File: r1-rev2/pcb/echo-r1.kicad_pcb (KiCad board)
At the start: 6 copper layers, 52 x 94 mm, 22 parts, among them J2 TYPE-C-31-M-12, J4 HP_3.5mm, J5 LO_3.5mm, SW1 A, SW10 SELECT, SW11 VOL+, SW12 VOL-, SW13 POWER, SW14 HOLD, SW2 B, SW3 X, SW4 Y, SW5 DPAD↑, SW6 DPAD↓, SW7 DPAD←, SW8 DPAD→, SW9 START

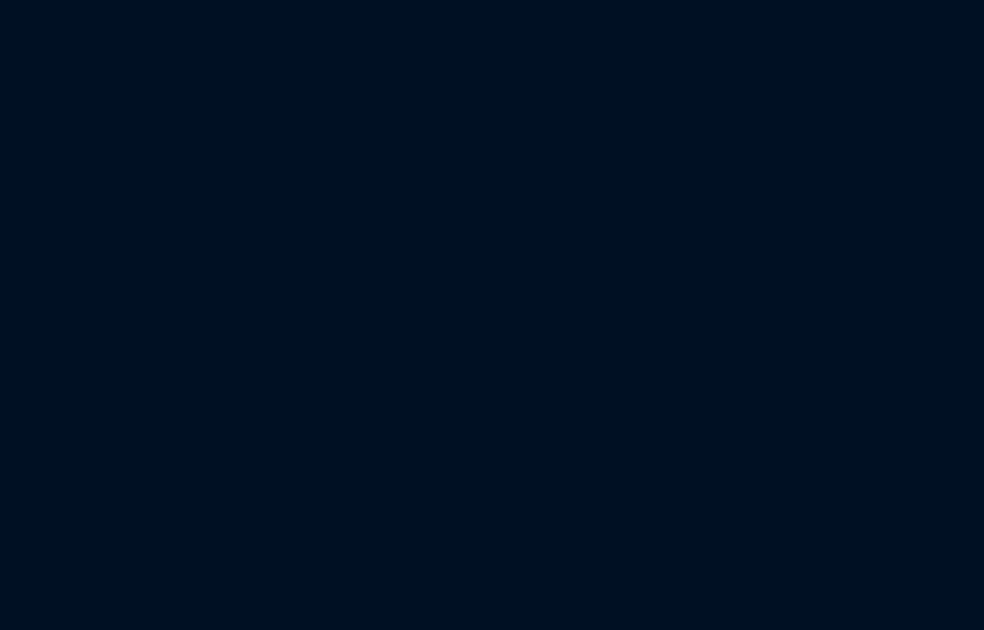
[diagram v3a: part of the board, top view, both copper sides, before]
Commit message: R1-Rev2: add LCD ribbon connector
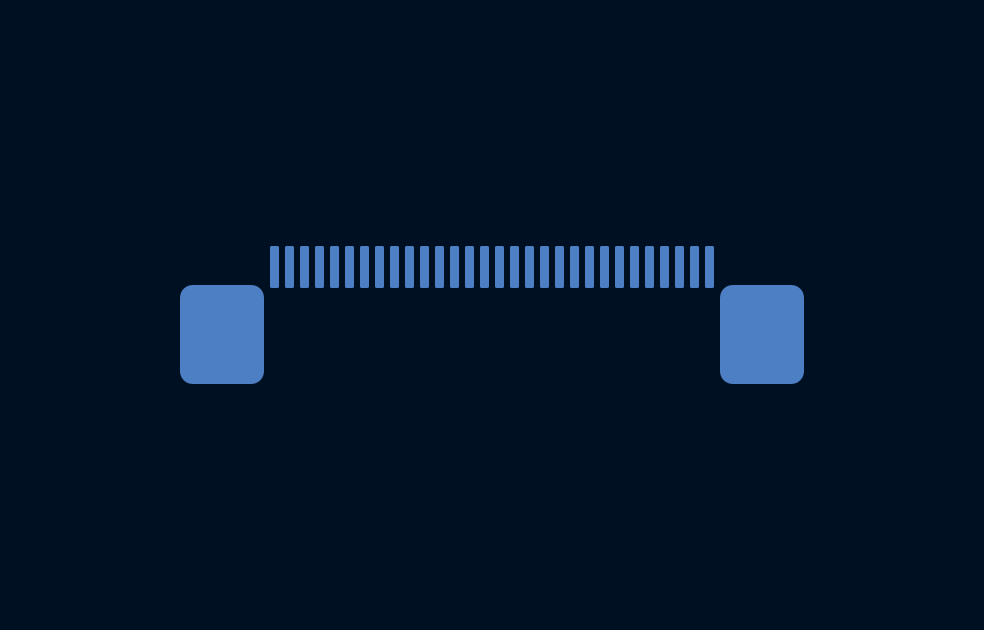
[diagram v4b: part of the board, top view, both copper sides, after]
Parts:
- added J7: AFC07-S30ECA-00, echoplayer:Conn_Jushuo_AFC07-S30ECA-00_RTL, B.Cu at (147.5, 74.3)

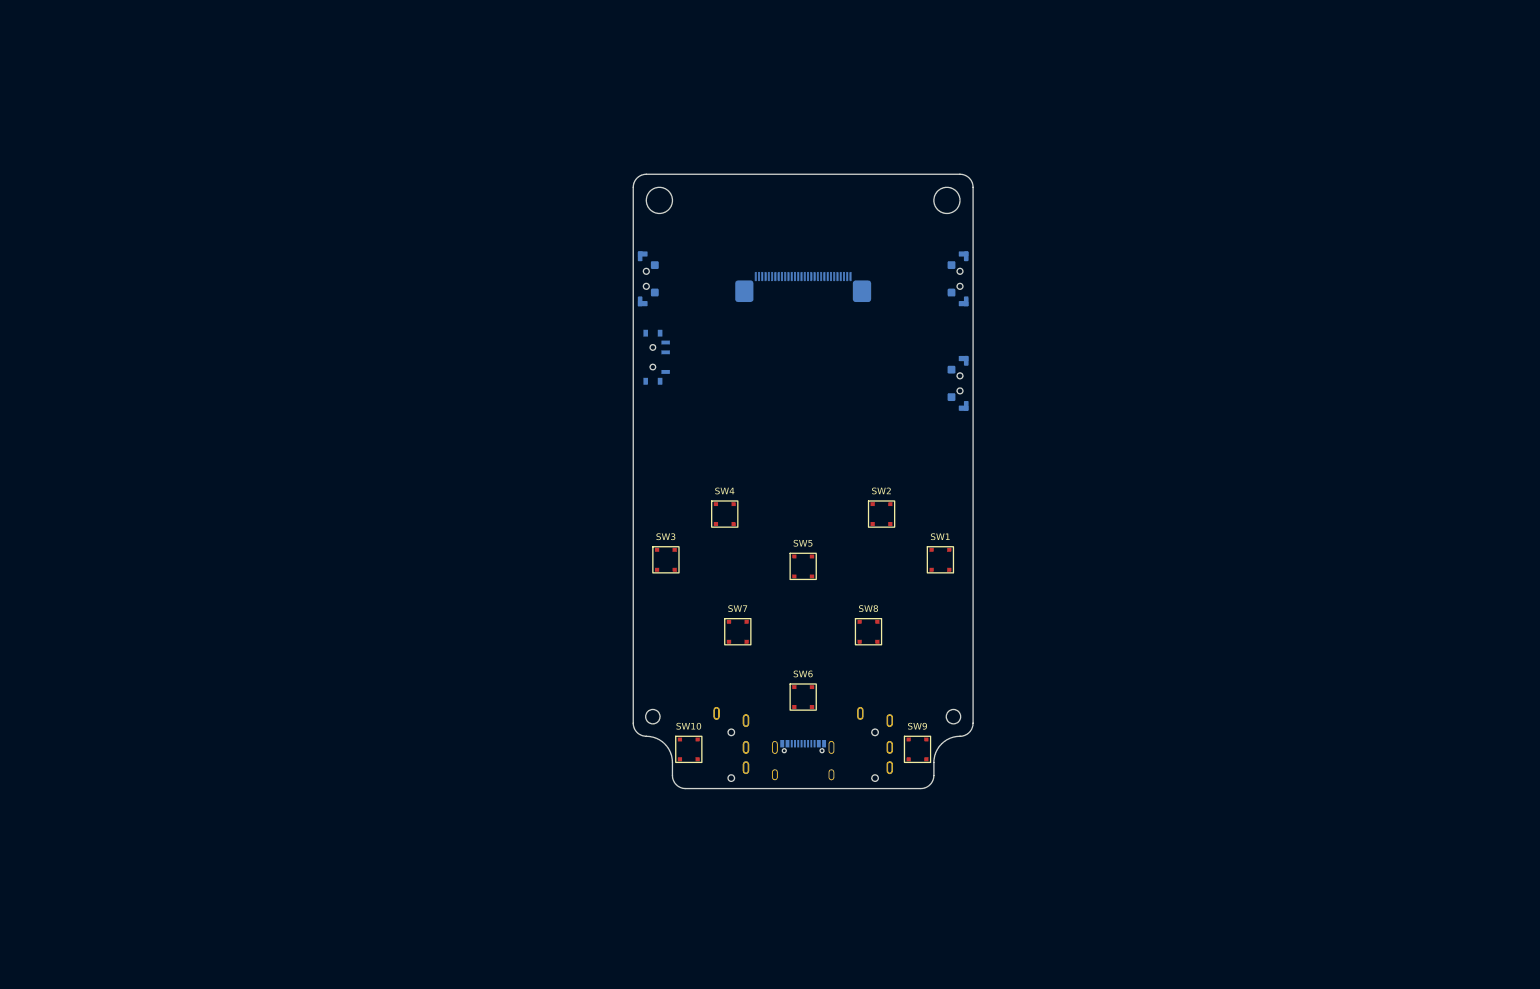
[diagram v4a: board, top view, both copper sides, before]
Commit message: R1-Rev2: updates to PCB layout, add HyperRAM routing
- Reannotate schematic and assign footprints for passives
- First try at HyperRAM routing
- Fixed incorrect W958D8NBYA5I pinout
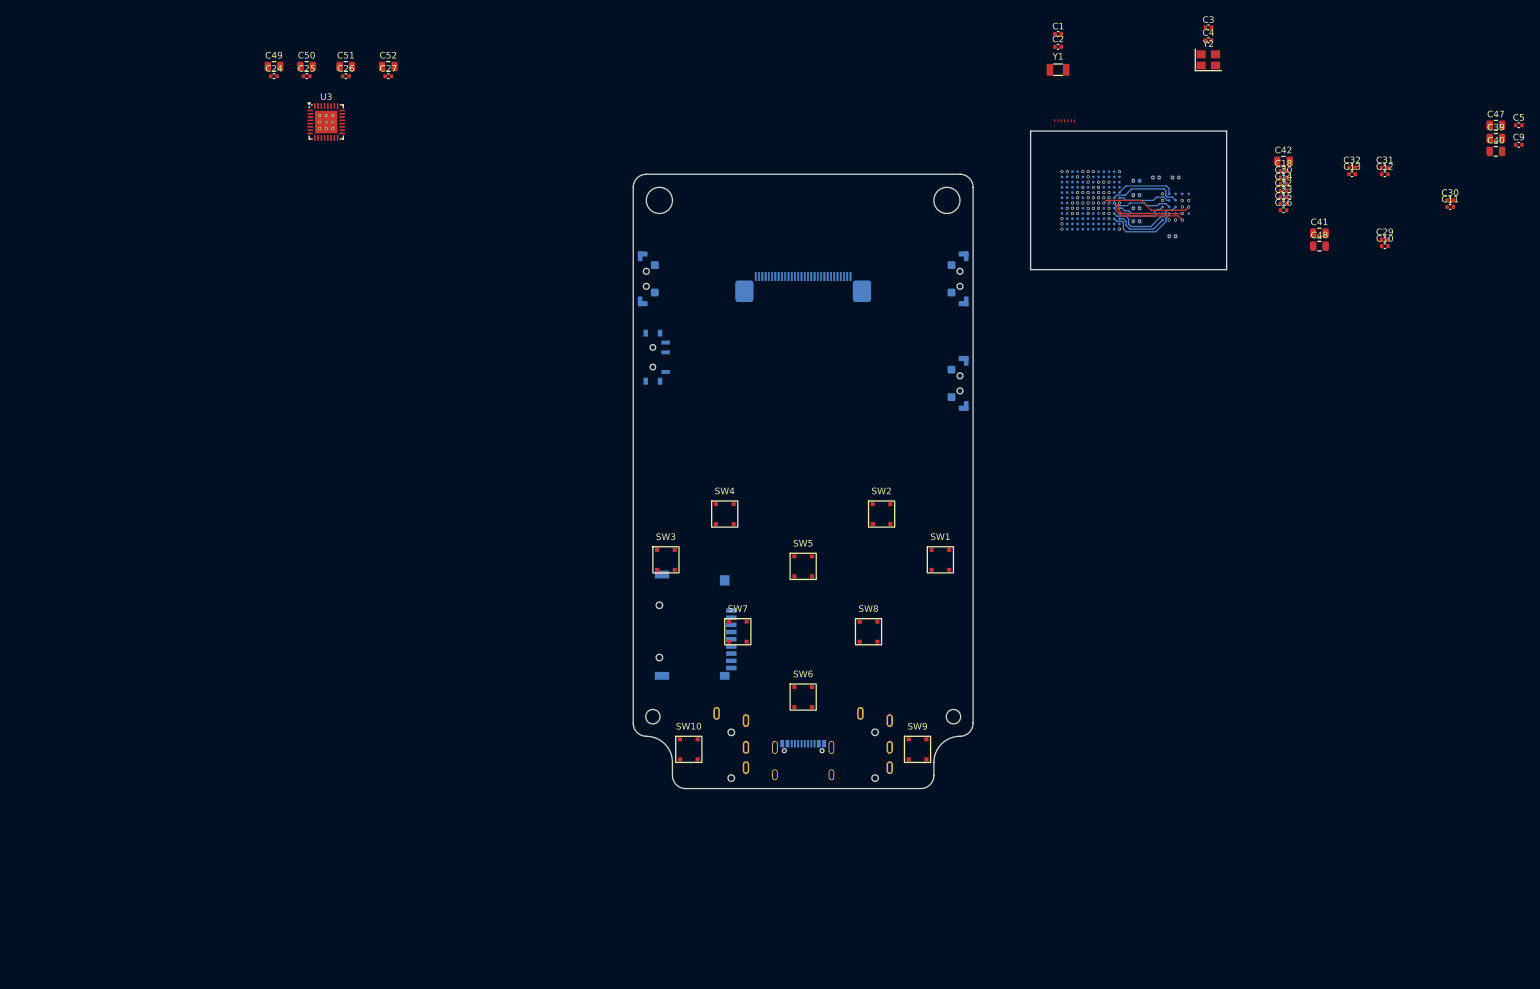
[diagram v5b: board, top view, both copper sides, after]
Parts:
- added C1: 10 pF, Capacitor_SMD:C_0402_1005Metric, F.Cu at (186.5, 36.5)
- added C10: 100 nF, Capacitor_SMD:C_0402_1005Metric, F.Cu at (236.5, 69.0)
- added C11: 100 nF, Capacitor_SMD:C_0402_1005Metric, F.Cu at (246.5, 63.0)
- added C12: 100 nF, Capacitor_SMD:C_0402_1005Metric, F.Cu at (236.5, 58.0)
- added C13: 100 nF, Capacitor_SMD:C_0402_1005Metric, F.Cu at (231.5, 58.0)
- added C14: 100 nF, Capacitor_SMD:C_0402_1005Metric, F.Cu at (221.0, 59.5)
- added C15: 100 nF, Capacitor_SMD:C_0402_1005Metric, F.Cu at (221.0, 62.5)
- added C16: 100 nF, Capacitor_SMD:C_0402_1005Metric, F.Cu at (221.0, 63.5)
- added C17: 100 nF, Capacitor_SMD:C_0402_1005Metric, B.Cu at (198.5, 65.2)
- added C18: 100 nF, Capacitor_SMD:C_0402_1005Metric, F.Cu at (221.0, 57.5)
- added C19: 100 nF, Capacitor_SMD:C_0402_1005Metric, B.Cu at (198.5, 63.2)
- added C2: 10 pF, Capacitor_SMD:C_0402_1005Metric, F.Cu at (186.5, 38.5)
- added C20: 100 nF, Capacitor_SMD:C_0402_1005Metric, F.Cu at (221.0, 58.5)
- added C21: 100 nF, Capacitor_SMD:C_0402_1005Metric, B.Cu at (198.5, 61.2)
- added C22: 100 nF, Capacitor_SMD:C_0402_1005Metric, F.Cu at (221.0, 60.5)
- added C23: 100 nF, Capacitor_SMD:C_0402_1005Metric, F.Cu at (221.0, 61.5)
- added C24: 100 nF, Capacitor_SMD:C_0402_1005Metric, F.Cu at (66.5, 43.0)
- added C25: 100 nF, Capacitor_SMD:C_0402_1005Metric, F.Cu at (71.5, 43.0)
- added C26: 100 nF, Capacitor_SMD:C_0402_1005Metric, F.Cu at (77.5, 43.0)
- added C27: 100 nF, Capacitor_SMD:C_0402_1005Metric, F.Cu at (84.0, 43.0)
- added C29: 1 µF, Capacitor_SMD:C_0402_1005Metric, F.Cu at (236.5, 68.0)
- added C3: 10 pF, Capacitor_SMD:C_0402_1005Metric, F.Cu at (209.5, 35.5)
- added C30: 1 µF, Capacitor_SMD:C_0402_1005Metric, F.Cu at (246.5, 62.0)
- added C31: 1 µF, Capacitor_SMD:C_0402_1005Metric, F.Cu at (236.5, 57.0)
- added C32: 1 µF, Capacitor_SMD:C_0402_1005Metric, F.Cu at (231.5, 57.0)
- added C33: 1 µF, Capacitor_SMD:C_0402_1005Metric, B.Cu at (198.5, 59.0)
- added C39: 4.7 µF, Capacitor_SMD:C_0805_2012Metric, F.Cu at (253.5, 52.5)
- added C4: 10 pF, Capacitor_SMD:C_0402_1005Metric, F.Cu at (209.5, 37.5)
- added C40: 4.7 µF, Capacitor_SMD:C_0805_2012Metric, F.Cu at (253.5, 54.5)
- added C41: 4.7 µF, Capacitor_SMD:C_0805_2012Metric, F.Cu at (226.5, 67.0)
- added C42: 4.7 µF, Capacitor_SMD:C_0805_2012Metric, F.Cu at (221.0, 56.0)
- added C47: 10 µF, Capacitor_SMD:C_0805_2012Metric, F.Cu at (253.5, 50.5)
- added C48: 10 µF, Capacitor_SMD:C_0805_2012Metric, F.Cu at (226.5, 69.0)
- added C49: 10 µF, Capacitor_SMD:C_0805_2012Metric, F.Cu at (66.5, 41.5)
- added C5: 220 pF, Capacitor_SMD:C_0402_1005Metric, F.Cu at (257.0, 50.5)
- added C50: 10 µF, Capacitor_SMD:C_0805_2012Metric, F.Cu at (71.5, 41.5)
- added C51: 10 µF, Capacitor_SMD:C_0805_2012Metric, F.Cu at (77.5, 41.5)
- added C52: 10 µF, Capacitor_SMD:C_0805_2012Metric, F.Cu at (84.0, 41.5)
- added C6: 100 nF, Capacitor_SMD:C_0402_1005Metric, B.Cu at (204.5, 58.5)
- added C7: 100 nF, Capacitor_SMD:C_0402_1005Metric, B.Cu at (204.0, 67.5)
- added C8: 100 nF, Capacitor_SMD:C_0402_1005Metric, B.Cu at (201.5, 58.5)
- added C9: 100 nF, Capacitor_SMD:C_0402_1005Metric, F.Cu at (257.0, 53.5)
- added J2: TF-115, echoplayer:microSD_XUNPU_TF-115, B.Cu at (129.5, 127.0)
- added NT1: NetTie_2, echoplayer:NetTie_0.15mm_SMD, F.Cu at (187.0, 49.8)
- added NT2: NetTie_2, echoplayer:NetTie_0.15mm_SMD, F.Cu at (187.5, 49.8)
- added NT3: NetTie_2, echoplayer:NetTie_0.15mm_SMD, F.Cu at (188.0, 49.8)
- added NT4: NetTie_2, echoplayer:NetTie_0.15mm_SMD, F.Cu at (188.5, 49.8)
- added NT5: NetTie_2, echoplayer:NetTie_0.15mm_SMD, F.Cu at (189.0, 49.8)
- added NT6: NetTie_2, echoplayer:NetTie_0.15mm_SMD, F.Cu at (186.0, 49.8)
- added NT7: NetTie_2, echoplayer:NetTie_0.15mm_SMD, F.Cu at (186.5, 49.8)
- added U1: STM32H7R3Z8Jx, Package_BGA:UFBGA-144_10x10mm_Layout12x12_P0.8mm, B.Cu at (191.5, 62.0)
- added U2: W958D8NBYA5I, echoplayer:TFBGA-24_6x8mm_Layout5x5_P1.0mm_Ball0.4mm, B.Cu at (204.5, 63.0)
- added U3: TLV320AIC3104, Package_DFN_QFN:Texas_RHB0032E_VQFN-32-1EP_5x5mm_P0.5mm_EP3.45x3.45mm_ThermalVias, F.Cu at (74.5, 50.0)
- added Y1: SC-32S32.768kHz20PPM12.5pF, Crystal:Crystal_SMD_3215-2Pin_3.2x1.5mm, F.Cu at (186.5, 42.0)
- added Y2: XTM32024000JT00351001, Crystal:Crystal_SMD_3225-4Pin_3.2x2.5mm, F.Cu at (209.5, 40.5)
- renumbered J2 to J1, J4 to J3, J5 to J4, J7 to J6
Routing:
- net +1V8: track 0.00 -> 26.2 mm, vias 0 -> 13
- net /xspi.cs: track 0.00 -> 14.0 mm, vias 0 -> 2
- net /xspi.dqs0: track 0.00 -> 12.2 mm
- net /xspi.ck-: track 0.00 -> 12.0 mm, vias 0 -> 2
- net /xspi.d1: track 0.00 -> 11.4 mm
- net /xspi.ck+: track 0.00 -> 11.1 mm, vias 0 -> 2
- net /xspi.d2: track 0.00 -> 11.1 mm
- net /xspi.d0: track 0.00 -> 9.23 mm
- net /xspi.d4: track 0.00 -> 8.98 mm
- net /xspi.d7: track 0.00 -> 8.19 mm
- net /xspi.d3: track 0.00 -> 8.18 mm
- net /xspi.d5: track 0.00 -> 7.35 mm
- net /xspi.d6: track 0.00 -> 6.93 mm
- net VBUS: vias 0 -> 2
- net Net-(U1-VCAP1): vias 0 -> 4
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- added copper zone on In3.Cu, net +1V8
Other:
- board size 52 x 94 mm -> 90.8 x 100.6 mm

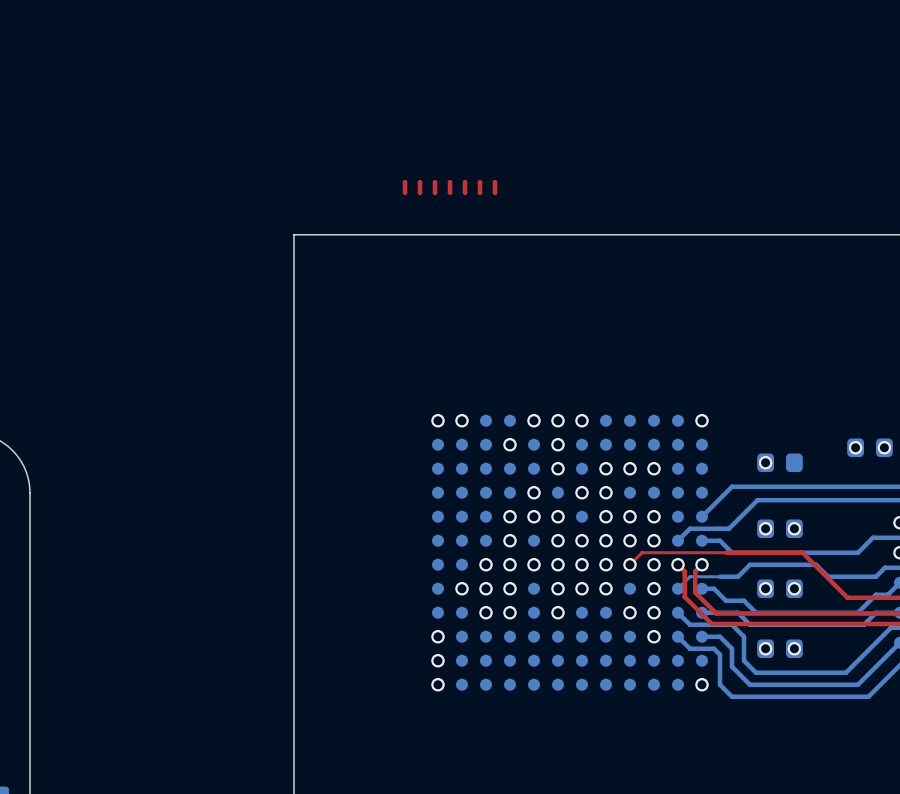
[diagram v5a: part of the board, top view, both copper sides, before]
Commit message: R1-Rev2: update USB D+/D- net ties to avoid USBHS stubs
The USB data lines have to be routed to both HS and FS PHYs
since only the FS PHY supports DFU mode. To minimize stub
length in HS operation, the data lines from the connector
should route through the FS pins first and terminate at the
HS pins.
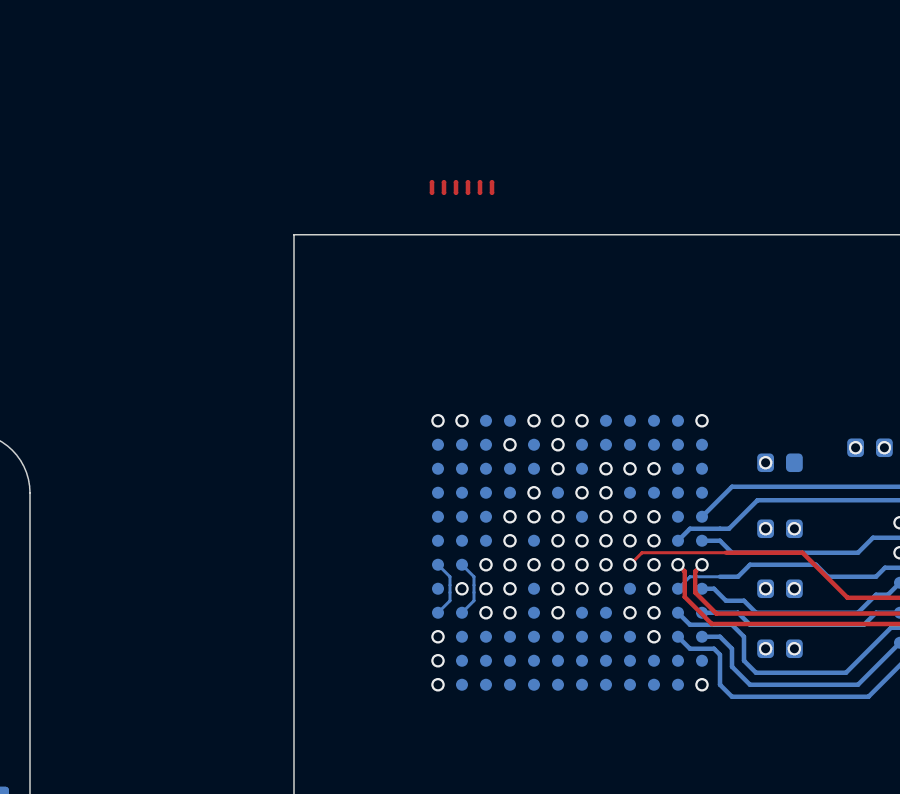
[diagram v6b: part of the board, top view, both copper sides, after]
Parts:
- removed NT2, NT3: NetTie_2, echoplayer:NetTie_0.15mm_SMD
- added NT10: NetTie_2, echoplayer:NetTie_0.15mm_SMD, F.Cu at (188.1, 49.8)
- added NT8: NetTie_2, echoplayer:NetTie_0.10mm_SMD, B.Cu at (188.3, 63.2)
- added NT9: NetTie_2, echoplayer:NetTie_0.10mm_SMD, B.Cu at (187.5, 63.2)
- moved NT6 0.90 mm to (186.9, 49.8)
- moved NT7 0.80 mm to (187.3, 49.8)
- moved NT1 0.70 mm to (187.7, 49.8)
- moved NT5 0.10 mm to (188.9, 49.8)
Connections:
- net Net-(NT5-Pad2) renamed /vddldo
- net Net-(U1-VCAP1) renamed /vcap
- U1 pad A7: /usb_fs_d+ -> /usb_d+
- U1 pad A9: /usb_d+ -> /usb_hs_d+
- U1 pad B7: /usb_fs_d- -> /usb_d-
- U1 pad B9: /usb_d- -> /usb_hs_d-
- U1 pad C8: /vfbsmps -> /dvdd
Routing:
- net /usb_d-: track 0.00 -> 0.84 mm
- net /usb_d+: track 0.00 -> 0.84 mm
- net /usb_hs_d-: track 0.00 -> 0.84 mm
- net /usb_hs_d+: track 0.00 -> 0.84 mm
- net /vfbsmps: vias 2 -> 1
- net /dvdd: vias 0 -> 1
